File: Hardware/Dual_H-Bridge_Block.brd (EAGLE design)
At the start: 30.5 x 44.5 mm, 27 parts, among them U1 TB6612FNG, U2 EDISON_CONNECTOR_FULLMOUNTING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, U3 EDISON_CONNECTOR_FULLHEADER, U4 TXB0108

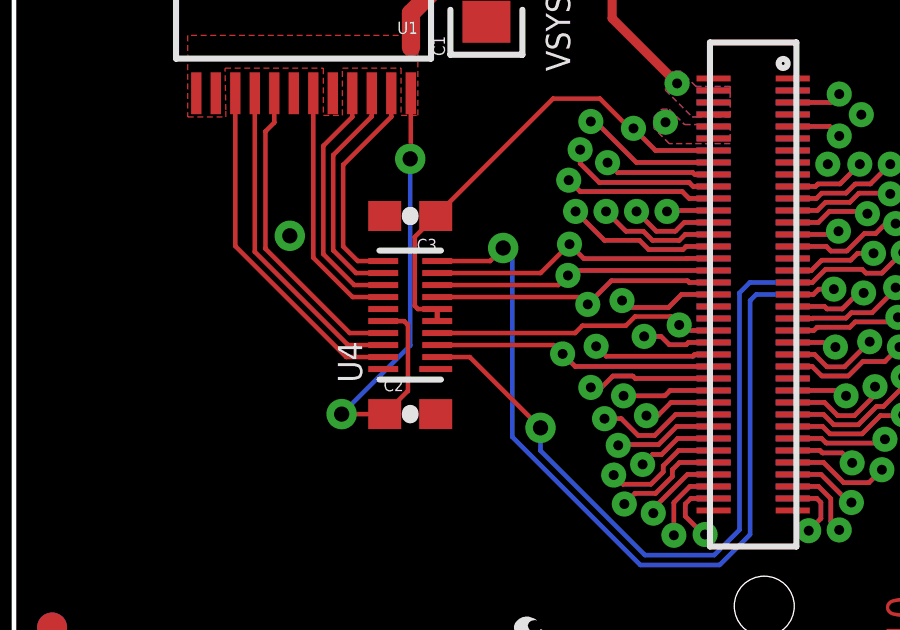
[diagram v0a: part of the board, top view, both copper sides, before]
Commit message: fixed level shifter pad jumper
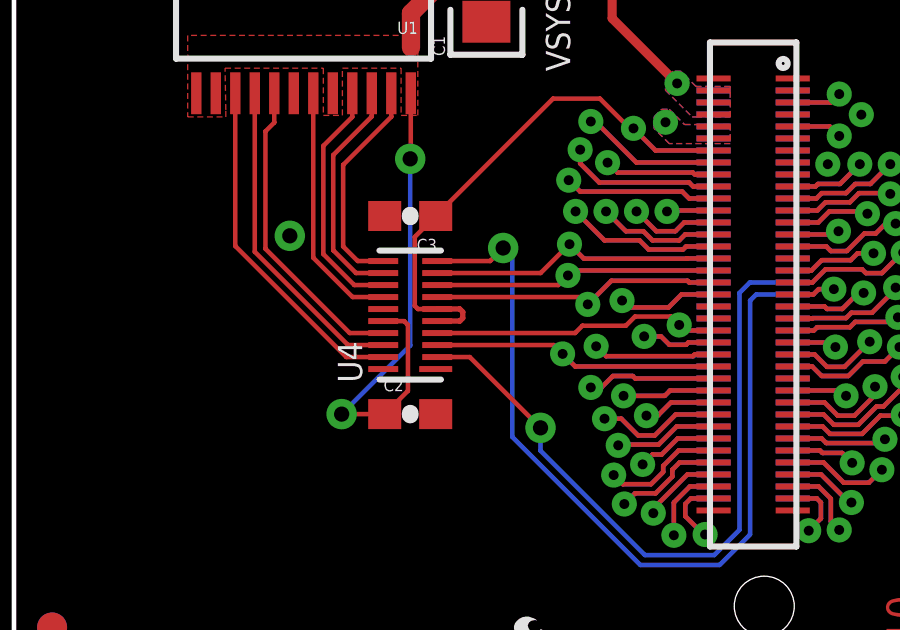
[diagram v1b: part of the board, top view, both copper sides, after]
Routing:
- net 1.8V: track 19.1 -> 20.6 mm
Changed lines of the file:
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@@
 <contactref element="C3" pad="1"/>
 <contactref element="U4" pad="6"/>
-<wire x1="14.108" y1="15.294" x2="14.108" y2="15.694" width="0.1778" layer="1"/>
 <wire x1="14.108" y1="15.694" x2="13.4652" y2="15.694" width="0.1524" layer="1"/>
 <wire x1="13.4652" y1="15.694" x2="13.3604" y2="15.7988" width="0.1524" layer="1"/>
@@
 <wire x1="13.3604" y1="15.7988" x2="13.3604" y2="18.0984" width="0.1524" layer="1"/>
 <wire x1="13.3604" y1="18.0984" x2="14.058" y2="18.796" width="0.1524" layer="1"/>
+<wire x1="14.108" y1="15.294" x2="14.8622" y2="15.294" width="0.1778" layer="1"/>
+<wire x1="14.8622" y1="15.294" x2="14.9606" y2="15.3924" width="0.1778" layer="1"/>
+<wire x1="14.9606" y1="15.3924" x2="14.9606" y2="15.5956" width="0.1778" layer="1"/>
+<wire x1="14.9606" y1="15.5956" x2="14.859" y2="15.6972" width="0.1778" layer="1"/>
+<wire x1="14.859" y1="15.6972" x2="14.1112" y2="15.6972" width="0.1778" layer="1"/>
+<wire x1="14.1112" y1="15.6972" x2="14.108" y2="15.694" width="0.1778" layer="1"/>
 </signal>
 <signal name="FW_RCVR">

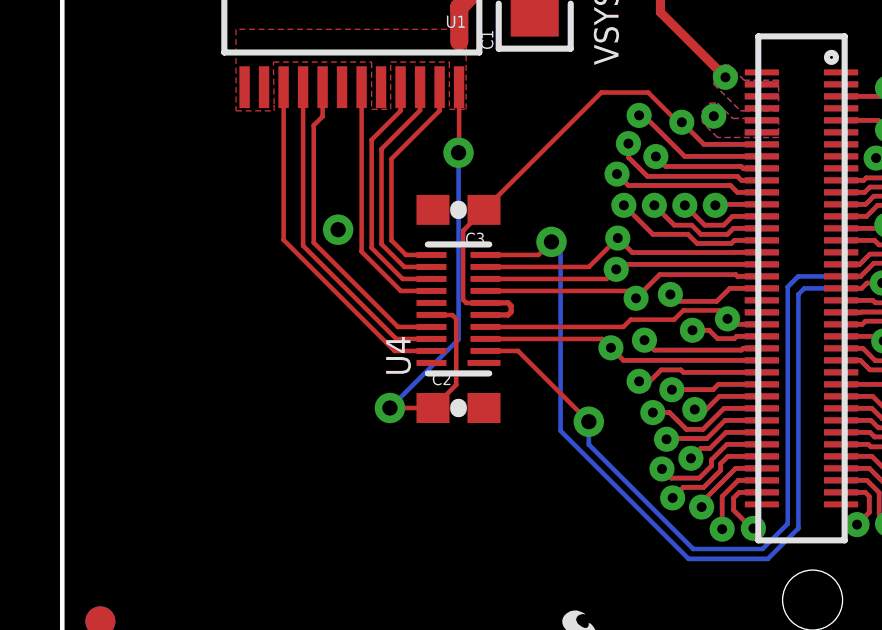
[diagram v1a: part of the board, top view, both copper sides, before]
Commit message: Changed Logic to vsys from vin
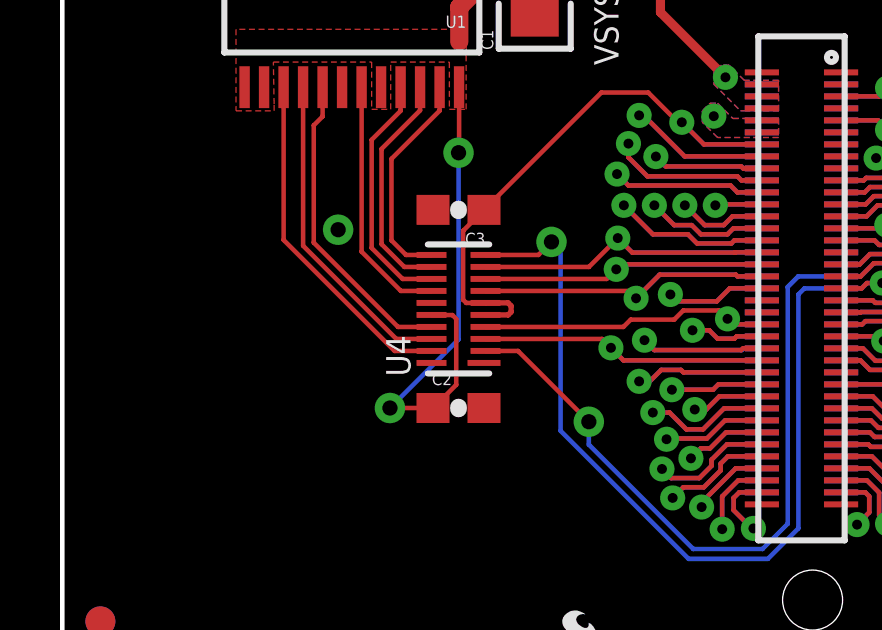
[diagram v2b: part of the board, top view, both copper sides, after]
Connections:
- net VIN: no longer U1.20, U4.16
- net VSYS: now also U1.20, U4.16
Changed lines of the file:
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@@
 <setting verticaltext="up"/>
 </settings>
-<grid distance="0.001" unitdist="inch" unit="inch" style="lines" multiple="1" display="yes" altdistance="0.005" altunitdist="inch" altunit="inch"/>
+<grid distance="0.05" unitdist="inch" unit="inch" style="lines" multiple="1" display="yes" altdistance="0.005" altunitdist="inch" altunit="inch"/>
 <layers>
 <layer number="1" name="Top" color="4" fill="1" visible="yes" active="yes"/>
-<layer number="2" name="Route2" color="1" fill="3" visible="yes" active="yes"/>
-<layer number="15" name="Route15" color="4" fill="6" visible="yes" active="yes"/>
+<layer number="2" name="Route2" color="1" fill="3" visible="no" active="yes"/>
+<layer number="15" name="Route15" color="4" fill="6" visible="no" active="yes"/>
 <layer number="16" name="Bottom" color="1" fill="1" visible="yes" active="yes"/>
 <layer number="17" name="Pads" color="2" fill="1" visible="yes" active="yes"/>
@@
 <layer number="23" name="tOrigins" color="15" fill="1" visible="yes" active="yes"/>
 <layer number="24" name="bOrigins" color="15" fill="1" visible="yes" active="yes"/>
-<layer number="25" name="tNames" color="7" fill="1" visible="yes" active="yes"/>
-<layer number="26" name="bNames" color="7" fill="1" visible="yes" active="yes"/>
-<layer number="27" name="tValues" color="7" fill="1" visible="yes" active="yes"/>
-<layer number="28" name="bValues" color="7" fill="1" visible="yes" active="yes"/>
-<layer number="29" name="tStop" color="7" fill="3" visible="yes" active="yes"/>
-<layer number="30" name="bStop" color="7" fill="6" visible="yes" active="yes"/>
-<layer number="31" name="tCream" color="7" fill="4" visible="yes" active="yes"/>
-<layer number="32" name="bCream" color="7" fill="5" visible="yes" active="yes"/>
-<layer number="39" name="tKeepout" color="4" fill="11" visible="yes" active="yes"/>
-<layer number="40" name="bKeepout" color="1" fill="11" visible="yes" active="yes"/>
-<layer number="41" name="tRestrict" color="4" fill="10" visible="yes" active="yes"/>
-<layer number="42" name="bRestrict" color="1" fill="10" visible="yes" active="yes"/>
-<layer number="43" name="vRestrict" color="2" fill="10" visible="yes" active="yes"/>
-<layer number="44" name="Drills" color="7" fill="1" visible="yes" active="yes"/>
+<layer number="25" name="tNames" color="7" fill="1" visible="no" active="yes"/>
+<layer number="26" name="bNames" color="7" fill="1" visible="no" active="yes"/>
+<layer number="27" name="tValues" color="7" fill="1" visible="no" active="yes"/>
+<layer number="28" name="bValues" color="7" fill="1" visible="no" active="yes"/>
+<layer number="29" name="tStop" color="7" fill="3" visible="no" active="yes"/>
+<layer number="30" name="bStop" color="7" fill="6" visible="no" active="yes"/>
+<layer number="31" name="tCream" color="7" fill="4" visible="no" active="yes"/>
+<layer number="32" name="bCream" color="7" fill="5" visible="no" active="yes"/>
+<layer number="39" name="tKeepout" color="4" fill="11" visible="no" active="yes"/>
+<layer number="40" name="bKeepout" color="1" fill="11" visible="no" active="yes"/>
+<layer number="41" name="tRestrict" color="4" fill="10" visible="no" active="yes"/>
+<layer number="42" name="bRestrict" color="1" fill="10" visible="no" active="yes"/>
+<layer number="43" name="vRestrict" color="2" fill="10" visible="no" active="yes"/>
+<layer number="44" name="Drills" color="7" fill="1" visible="no" active="yes"/>
 <layer number="45" name="Holes" color="7" fill="1" visible="yes" active="yes"/>
-<layer number="46" name="Milling" color="3" fill="1" visible="yes" active="yes"/>
+<layer number="46" name="Milling" color="3" fill="1" visible="no" active="yes"/>
 <layer number="51" name="tDocu" color="6" fill="1" visible="yes" active="yes"/>
 <layer number="3" name="Route3" color="4" fill="3" visible="no" active="no"/>
@@
 <layer number="251" name="SMDround" color="12" fill="11" visible="no" active="no"/>
 <layer number="254" name="cooling" color="7" fill="1" visible="no" active="no"/>
-<layer number="255" name="routoute" color="7" fill="1" visible="yes" active="yes"/>
+<layer number="255" name="routoute" color="7" fill="1" visible="no" active="no"/>
 </layers>
 <board>
@@
 <vertex x="22.606" y="22.098"/>
 </polygon>
+<contactref element="U4" pad="16"/>
+<contactref element="U1" pad="20"/>
+<wire x1="12.308" y1="15.294" x2="10.627" y2="22.887" width="0" layer="19" extent="1-1"/>
+<wire x1="19.939" y1="25.3814" x2="10.627" y2="22.887" width="0" layer="19" extent="1-1"/>
 </signal>
 <signal name="3.3V">
@@
 <contactref element="U1" pad="14"/>
 <contactref element="U1" pad="24"/>
-<contactref element="U1" pad="20"/>
-<contactref element="U4" pad="16"/>
 <contactref element="C2" pad="1"/>
 <contactref element="C1" pad="A"/>
@@
 <wire x1="19.939" y1="35.179" x2="15.748" y2="30.988" width="0.6096" layer="1"/>
 <wire x1="15.748" y1="30.988" x2="15.748" y2="28.07" width="0.6096" layer="1"/>
-<wire x1="12.308" y1="15.294" x2="12.3112" y2="15.2908" width="0.1524" layer="1"/>
 <wire x1="12.3112" y1="15.2908" x2="13.0048" y2="15.2908" width="0.1524" layer="1"/>
 <wire x1="13.0048" y1="15.2908" x2="13.1318" y2="15.1638" width="0.1524" layer="1"/>

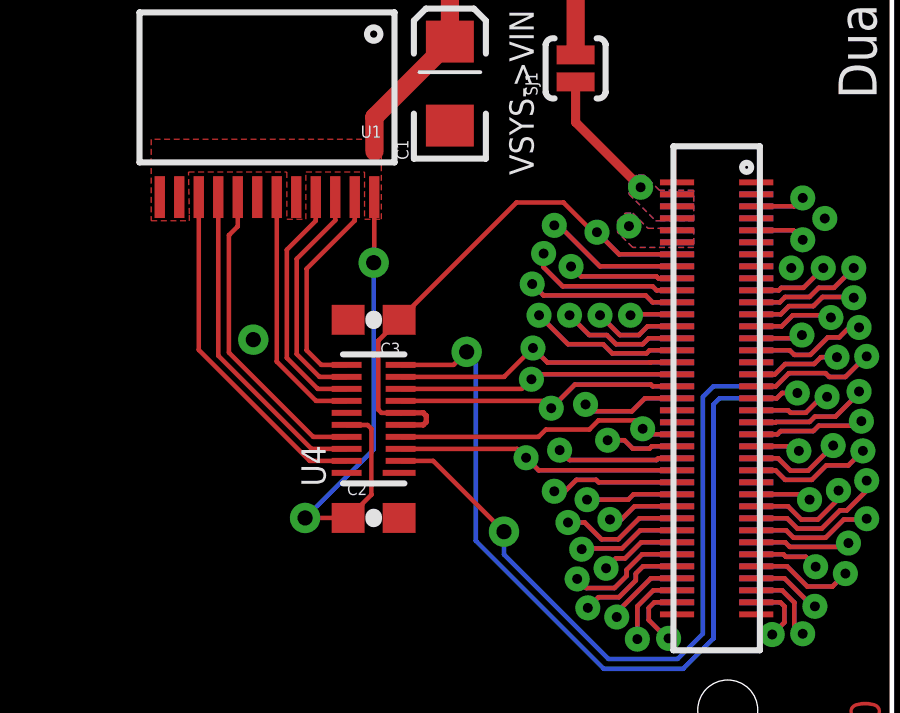
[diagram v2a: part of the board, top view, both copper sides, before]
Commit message: finishing routing and cleaning up pads
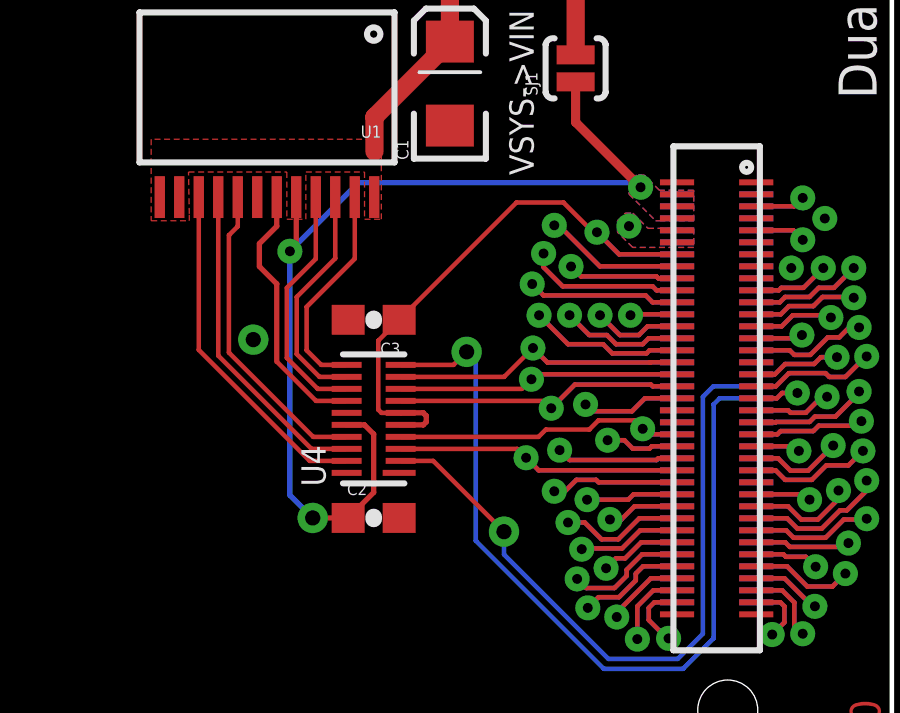
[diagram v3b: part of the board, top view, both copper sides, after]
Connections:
- net VIN: no longer C2.1
- net VSYS: now also C2.1
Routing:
- net VSYS: track 4.41 -> 33.6 mm, vias 1 -> 3
- net VIN: track 39.1 -> 21.9 mm, vias 2 -> 0
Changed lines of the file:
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@@
 <setting verticaltext="up"/>
 </settings>
-<grid distance="0.05" unitdist="inch" unit="inch" style="lines" multiple="1" display="yes" altdistance="0.005" altunitdist="inch" altunit="inch"/>
+<grid distance="0.01" unitdist="inch" unit="inch" style="lines" multiple="1" display="yes" altdistance="0.005" altunitdist="inch" altunit="inch"/>
 <layers>
 <layer number="1" name="Top" color="4" fill="1" visible="yes" active="yes"/>
@@
 <contactref element="C3" pad="2"/>
 <contactref element="C1" pad="C"/>
+<via x="9.1948" y="18.1356" extent="1-16" drill="0.508"/>
 <contactref element="C2" pad="2"/>
-<via x="9.1948" y="18.1356" extent="1-16" drill="0.508"/>
 </signal>
 <signal name="VSYS">
@@
 <contactref element="U4" pad="16"/>
 <contactref element="U1" pad="20"/>
-<wire x1="12.308" y1="15.294" x2="10.627" y2="22.887" width="0" layer="19" extent="1-1"/>
-<wire x1="19.939" y1="25.3814" x2="10.627" y2="22.887" width="0" layer="19" extent="1-1"/>
+<contactref element="C2" pad="1"/>
+<wire x1="10.627" y1="22.887" x2="10.627" y2="21.295" width="0.1778" layer="1"/>
+<wire x1="10.627" y1="21.295" x2="10.414" y2="21.082" width="0.1778" layer="1"/>
+<via x="10.414" y="21.082" extent="1-16" drill="0.3302"/>
+<wire x1="10.414" y1="21.082" x2="10.414" y2="12.954" width="0.1778" layer="16"/>
+<wire x1="10.414" y1="12.954" x2="11.176" y2="12.192" width="0.1778" layer="16"/>
+<via x="11.176" y="12.192" extent="1-16" drill="0.508"/>
+<wire x1="11.176" y1="12.192" x2="12.358" y2="12.192" width="0.1778" layer="1"/>
+<wire x1="12.308" y1="15.294" x2="12.9" y2="15.294" width="0.1778" layer="1"/>
+<wire x1="12.9" y1="15.294" x2="13.208" y2="14.986" width="0.1778" layer="1"/>
+<wire x1="13.208" y1="14.986" x2="13.208" y2="13.042" width="0.1778" layer="1"/>
+<wire x1="13.208" y1="13.042" x2="12.358" y2="12.192" width="0.1778" layer="1"/>
+<wire x1="10.414" y1="21.082" x2="12.7" y2="23.368" width="0.1778" layer="16"/>
+<wire x1="12.7" y1="23.368" x2="21.9524" y2="23.368" width="0.1778" layer="16"/>
+<wire x1="21.9524" y1="23.368" x2="22.1054" y2="23.215" width="0.1778" layer="16"/>
 </signal>
 <signal name="3.3V">
@@
 <contactref element="U1" pad="19"/>
 <contactref element="U4" pad="14"/>
-<wire x1="9.977" y1="22.887" x2="9.977" y2="17.4042" width="0.1524" layer="1"/>
 <wire x1="9.977" y1="17.4042" x2="11.2872" y2="16.094" width="0.1524" layer="1"/>
 <wire x1="11.2872" y1="16.094" x2="12.308" y2="16.094" width="0.1524" layer="1"/>
+<wire x1="9.977" y1="22.887" x2="9.977" y2="21.915" width="0.1778" layer="1"/>
+<wire x1="9.977" y1="21.915" x2="9.398" y2="21.336" width="0.1778" layer="1"/>
+<wire x1="9.398" y1="21.336" x2="9.398" y2="20.574" width="0.1778" layer="1"/>
+<wire x1="9.398" y1="20.574" x2="9.977" y2="19.995" width="0.1778" layer="1"/>
+<wire x1="9.977" y1="19.995" x2="9.977" y2="17.4042" width="0.1778" layer="1"/>
 </signal>
 <signal name="N$11">
@@
 <contactref element="U1" pad="21"/>
 <contactref element="U4" pad="13"/>
-<wire x1="11.277" y1="22.887" x2="11.277" y2="22.0974" width="0.1524" layer="1"/>
-<wire x1="11.277" y1="22.0974" x2="10.3124" y2="21.1328" width="0.1524" layer="1"/>
-<wire x1="10.3124" y1="21.1328" x2="10.3124" y2="17.526" width="0.1524" layer="1"/>
+<wire x1="11.277" y1="22.887" x2="11.277" y2="20.8274" width="0.1524" layer="1"/>
+<wire x1="11.277" y1="20.8274" x2="10.3124" y2="19.8628" width="0.1524" layer="1"/>
+<wire x1="10.3124" y1="19.8628" x2="10.3124" y2="17.526" width="0.1524" layer="1"/>
 <wire x1="10.3124" y1="17.526" x2="11.3444" y2="16.494" width="0.1524" layer="1"/>
 <wire x1="11.3444" y1="16.494" x2="12.308" y2="16.494" width="0.1524" layer="1"/>
@@
 <contactref element="U1" pad="22"/>
 <contactref element="U4" pad="12"/>
-<wire x1="11.927" y1="22.887" x2="11.927" y2="22.1124" width="0.1524" layer="1"/>
-<wire x1="11.927" y1="22.1124" x2="10.6426" y2="20.828" width="0.1524" layer="1"/>
-<wire x1="10.6426" y1="20.828" x2="10.6426" y2="17.653" width="0.1524" layer="1"/>
+<wire x1="11.927" y1="22.887" x2="11.927" y2="20.8424" width="0.1524" layer="1"/>
+<wire x1="11.927" y1="20.8424" x2="10.6426" y2="19.558" width="0.1524" layer="1"/>
+<wire x1="10.6426" y1="19.558" x2="10.6426" y2="17.653" width="0.1524" layer="1"/>
 <wire x1="10.6426" y1="17.653" x2="11.4016" y2="16.894" width="0.1524" layer="1"/>
 <wire x1="11.4016" y1="16.894" x2="12.308" y2="16.894" width="0.1524" layer="1"/>
@@
 <contactref element="U1" pad="14"/>
 <contactref element="U1" pad="24"/>
-<contactref element="C2" pad="1"/>
 <contactref element="C1" pad="A"/>
 <contactref element="D1" pad="C"/>
@@
 <wire x1="19.939" y1="35.179" x2="15.748" y2="30.988" width="0.6096" layer="1"/>
 <wire x1="15.748" y1="30.988" x2="15.748" y2="28.07" width="0.6096" layer="1"/>
-<wire x1="12.3112" y1="15.2908" x2="13.0048" y2="15.2908" width="0.1524" layer="1"/>
-<wire x1="13.0048" y1="15.2908" x2="13.1318" y2="15.1638" width="0.1524" layer="1"/>
-<wire x1="13.1318" y1="15.1638" x2="13.1318" y2="12.9658" width="0.1524" layer="1"/>
-<wire x1="13.1318" y1="12.9658" x2="12.358" y2="12.192" width="0.1524" layer="1"/>
 <polygon width="0.1524" layer="1">
 <vertex x="5.7912" y="22.098"/>
@@
 <wire x1="15.748" y1="28.07" x2="13.2334" y2="25.5554" width="0.6096" layer="1"/>
 <wire x1="13.2334" y1="25.5554" x2="13.2334" y2="24.4094" width="0.6096" layer="1"/>
-<wire x1="13.227" y1="22.887" x2="13.227" y2="20.72" width="0.1524" layer="1"/>
-<wire x1="13.227" y1="20.72" x2="13.208" y2="20.701" width="0.1524" layer="1"/>
-<via x="13.208" y="20.701" extent="1-16" drill="0.508"/>
-<wire x1="13.208" y1="20.701" x2="13.208" y2="14.478" width="0.1524" layer="16"/>
-<wire x1="13.208" y1="14.478" x2="10.922" y2="12.192" width="0.1524" layer="16"/>
-<via x="10.922" y="12.192" extent="1-16" drill="0.508"/>
-<wire x1="10.922" y1="12.192" x2="12.358" y2="12.192" width="0.1524" layer="1"/>
 </signal>
 <signal name="N$3">
@@
 <contactref element="U1" pad="23"/>
 <contactref element="U4" pad="11"/>
-<wire x1="12.577" y1="22.887" x2="12.577" y2="22.102" width="0.1524" layer="1"/>
-<wire x1="12.577" y1="22.102" x2="10.9728" y2="20.4978" width="0.1524" layer="1"/>
-<wire x1="10.9728" y1="20.4978" x2="10.9728" y2="17.78" width="0.1524" layer="1"/>
+<wire x1="12.577" y1="22.887" x2="12.577" y2="20.832" width="0.1524" layer="1"/>
+<wire x1="12.577" y1="20.832" x2="10.9728" y2="19.2278" width="0.1524" layer="1"/>
+<wire x1="10.9728" y1="19.2278" x2="10.9728" y2="17.78" width="0.1524" layer="1"/>
 <wire x1="10.9728" y1="17.78" x2="11.4588" y2="17.294" width="0.1524" layer="1"/>
 <wire x1="11.4588" y1="17.294" x2="12.308" y2="17.294" width="0.1524" layer="1"/>
